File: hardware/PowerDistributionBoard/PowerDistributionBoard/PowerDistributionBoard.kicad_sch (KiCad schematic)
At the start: 117 parts, among them J1 Battery, J10 MOTOR2_PWR, J11 Router, J2 FAN 1, J3 FAN 2, J4 FAN 3, J5 FAN 4, J6 Inverter, J7 Control Board, J8 Conn_01x02, J9 MOTOR1_PWR, Q1 Q_NMOS_GDS, Q10 TK100E10N1,S1X, Q2 Q_NPN_EBC, Q3 Q_NMOS_GSD, Q4 Q_NMOS_GSD, Q5 Q_NPN_EBC, Q6 Q_NMOS_GSD, Q7 Q_NMOS_GSD, Q8 DMN62D0U-13, Q9 TK100E10N1,S1X, SW1 SW_SPDT, U1 LT1641-1, U2 MAX6643LBBAEET, U3 MAX6643LBBAEET, U4 MC74HC20ADG, U5 KSTW004A2B41Z, U6 AP2210N-3.3TRG1, U7 R-78B9.0-1.0

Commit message: Power Board Schematic Revision Done, Fix Lora Symbol and Update Control Board Routing
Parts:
- removed F1: 1A, PDBLib:0679L1000-05, symbol Device:Fuse
- added F?: 2A, PDBLib:3557-2, symbol Device:Fuse
- added F? (x2): 10A, PDBLib:3557-2, symbol Device:Fuse
- added F?: 25A, PDBLib:3557-2, symbol Device:Fuse
- added F? (x2): 1A, PDBLib:3557-2, symbol Device:Fuse
- C3: value 100p -> 1n
- D10, D9: footprint Package_TO_SOT_THT:TO-247-2_Horizontal_TabDown -> PDBLib:VS-15AWL06FNTR-M3; Digikey APT60DQ60BG-ND -> VS-15AWL06FNTR-M3GICT-ND; LCSC (none) -> C2838505
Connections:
- net +12V: now also F?.2; no longer D?.1 (K), J7.1 (Pin_1)
- net +48V: now also F?.2, F?.2, F?.2, F?.2; no longer C17.1, D10.1 (K), D9.1 (K), D?.1 (K), J10.1 (Pin_1), J6.1 (Pin_1), J9.1 (Pin_1)
- net +9V: now also F?.2; no longer D?.1 (K), J11.1 (Pin_1)
- net at C9.1, U5.1 (VIN+): now also F?.1
- new net: D?.1 (K), F?.1, J7.1 (Pin_1)
- new net: D10.1 (K), F?.1, J10.1 (Pin_1)
- new net: C17.1, D?.1 (K), F?.1, J6.1 (Pin_1)
- new net: D9.1 (K), F?.1, J9.1 (Pin_1)
- new net: D?.1 (K), F?.1, J11.1 (Pin_1)
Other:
- note added: "REVIEW V0.2"
- note removed: "REVIEW V0.1"
- moved on the sheet: C17, D?, J11, J6, J7

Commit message: PDB Layout
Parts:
- added R44: 4.7k, Resistor_SMD:R_0805_2012Metric, symbol Device:R_US
- C17, C9: footprint Capacitor_THT:CP_Radial_D12.5mm_P5.00mm -> Capacitor_THT:CP_Radial_D10.0mm_P5.00mm; Digikey 4191-PF2D330MCE1212F3-ND -> 1189-2207-ND; LCSC (none) -> C159830
- J11, J7: footprint Connector_Molex:Molex_Micro-Fit_3.0_43650-0200_1x02_P3.00mm_Horizontal -> Connector_Molex:Molex_Micro-Fit_3.0_43650-0215_1x02_P3.00mm_Vertical; Digikey WM1860-ND -> WM1917-ND
- R33: value 1k -> 4.7k
- gave numbers to parts that had none: 11
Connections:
- net ESTOP: now also R44.2
- net GND: now also R44.1

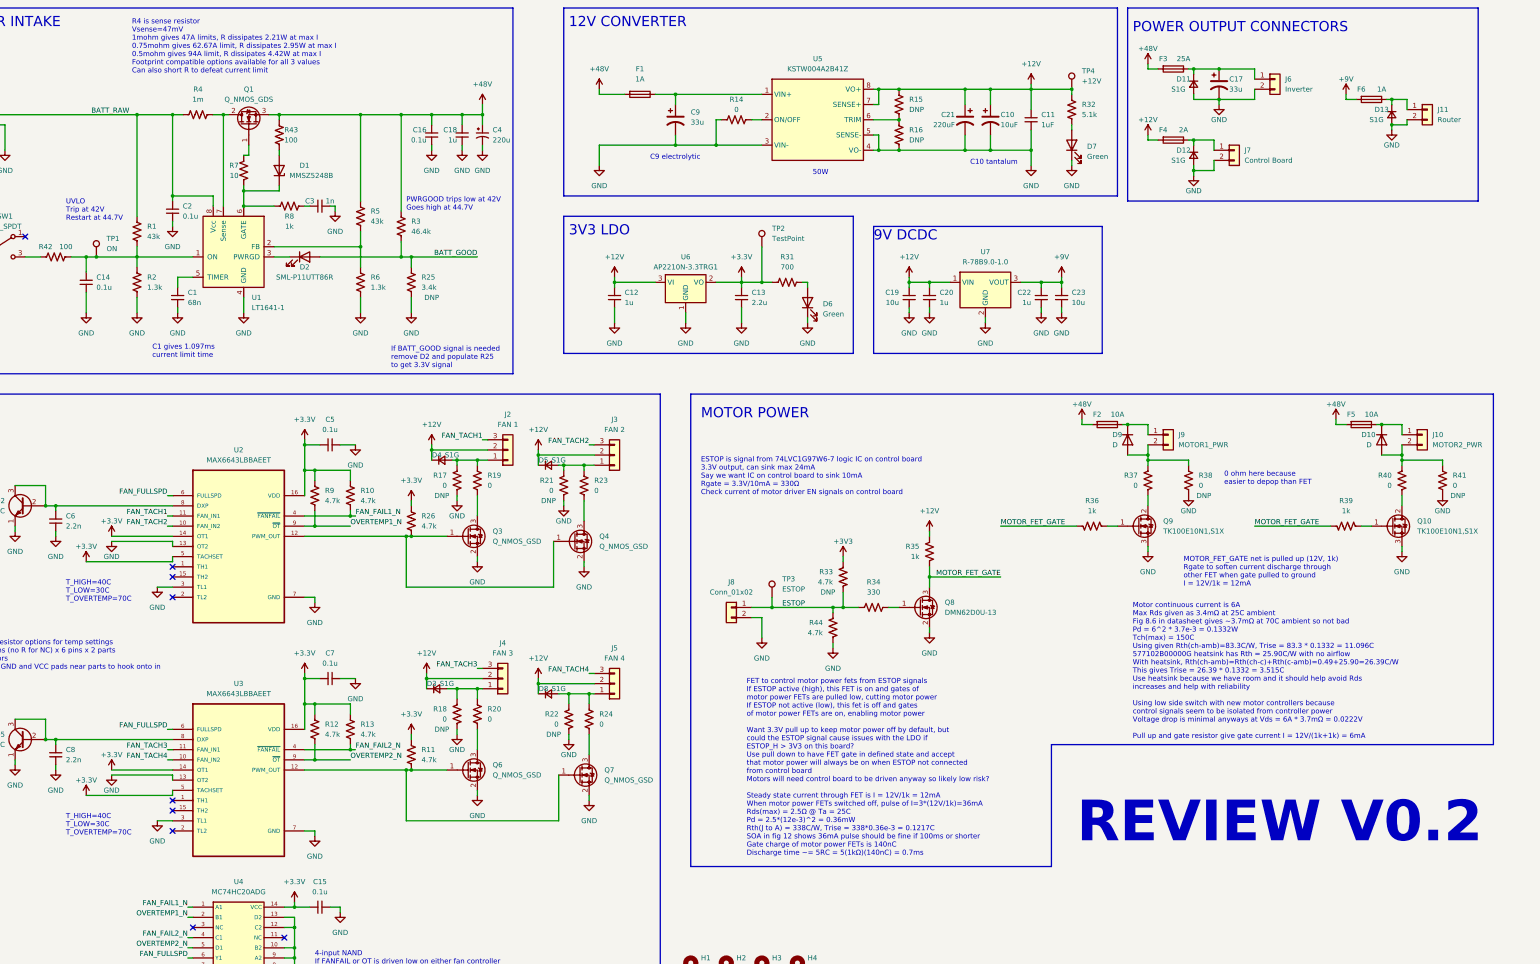
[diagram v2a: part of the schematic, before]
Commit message: PDB routing V2 first pass
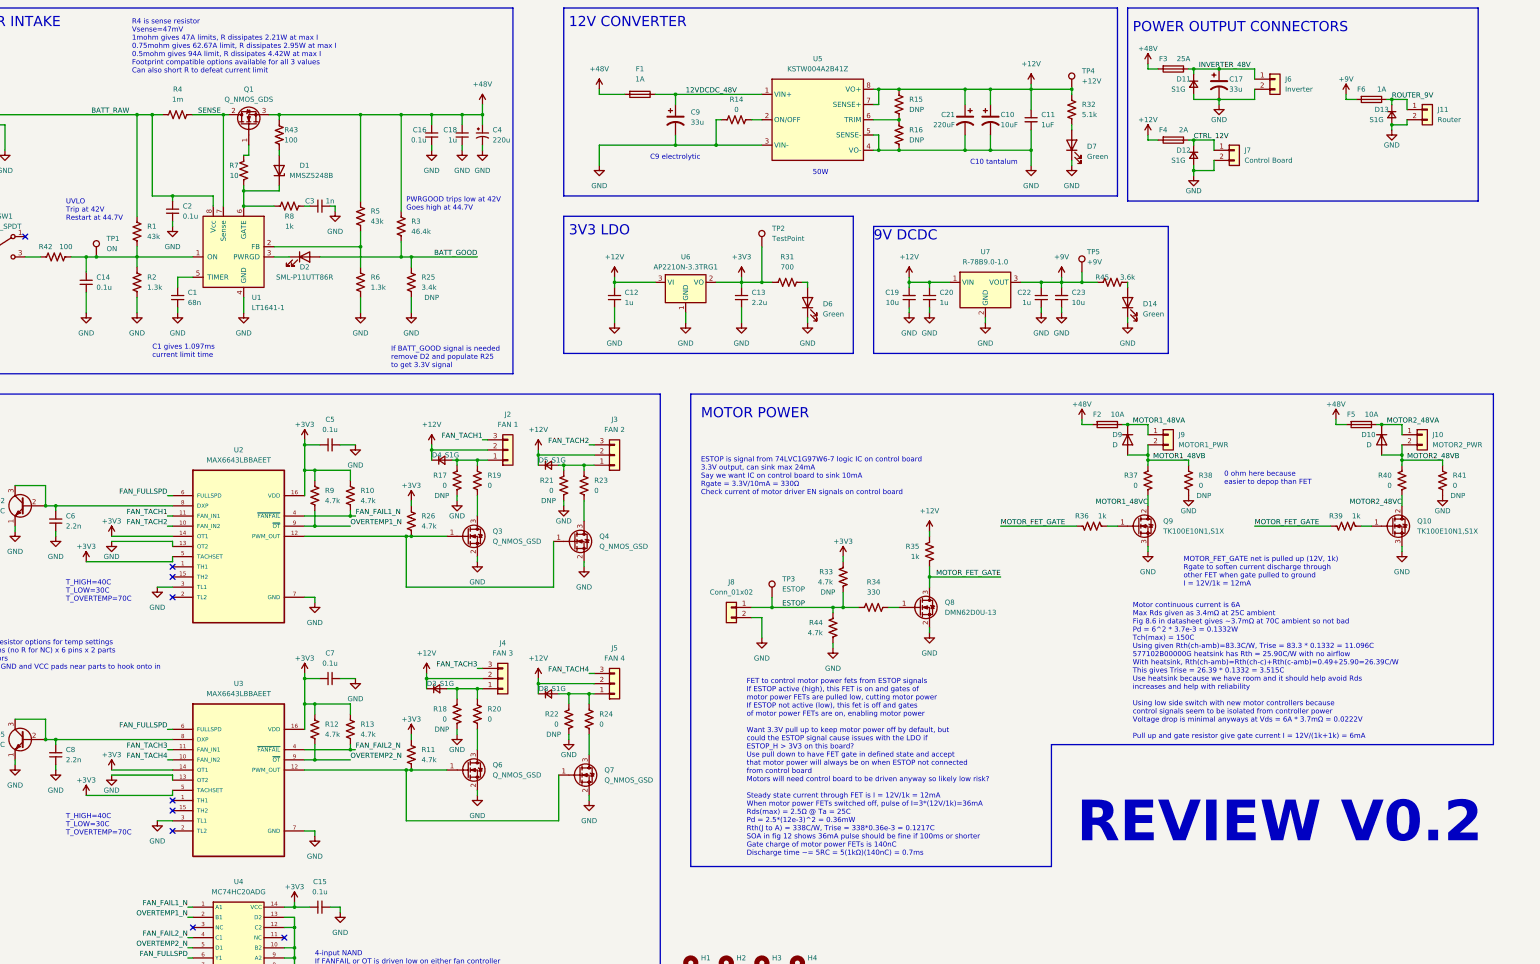
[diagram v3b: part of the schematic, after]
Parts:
- added D14: Green, LED_SMD:LED_0805_2012Metric_Pad1.15x1.40mm_HandSolder, symbol Device:LED
- added R45: 3.6k, Resistor_SMD:R_0805_2012Metric, symbol Device:R_US
- added TP5: +9V, TestPoint:TestPoint_Pad_D1.0mm, symbol Connector:TestPoint
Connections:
- net +3.3V is gone; now on net +3V3: C13.1, C15.1, C5.2, C7.2, R10.1, R11.1, R12.1, R13.1, R26.1, R31.2, R9.1, TP2.1, U2.14 (OT1), U2.16 (VDD), U2.5 (TACHSET), U3.14 (OT1), U3.16 (VDD), U3.5 (TACHSET), U4.14 (VCC), U6.2 (VO)
- net +9V: now also R45.2, TP5.1
- net GND: now also D14.1 (K)
- net CTRL_12V: now reaches D12.1 (K), F4.1, J7.1 (Pin_1)
- net MOTOR2_48VA: now reaches D10.1 (K), F5.1, J10.1 (Pin_1)
- net INVERTER_48V: now reaches C17.1, D11.1 (K), F3.1, J6.1 (Pin_1)
- net MOTOR2_48VC: now reaches Q10.2 (D), R40.1
- net MOTOR2_48VB: now reaches D10.2 (A), J10.2 (Pin_2), R40.2, R41.1
- net ROUTER_9V: now reaches D13.1 (K), F6.1, J11.1 (Pin_1)
- net SENSE: now reaches Q1.2 (D), R4.1, U1.7 (Sense)
- net MOTOR1_48VA: now reaches D9.1 (K), F2.1, J9.1 (Pin_1)
- net 12VDCDC_48V: now reaches C9.1, F1.1, U5.1 (VIN+)
- net MOTOR1_48VC: now reaches Q9.2 (D), R37.1
- net MOTOR1_48VB: now reaches D9.2 (A), J9.2 (Pin_2), R37.2, R38.1
- new net: D14.2 (A), R45.1
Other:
- moved on the sheet: R4

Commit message: Last things
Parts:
- U1: footprint Package_SO:SOIC-8_3.9x4.9mm_P1.27mm -> PDBLib:LT1641-1CS8#TRPBF
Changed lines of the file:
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@@
       (effects (font (size 1.27 1.27)) (justify left))
     )
-    (property "Footprint" "Package_SO:SOIC-8_3.9x4.9mm_P1.27mm" (id 2) (at 90.17 91.44 0)
+    (property "Footprint" "PDBLib:LT1641-1CS8#TRPBF" (id 2) (at 90.17 91.44 0)
       (effects (font (size 1.27 1.27)) hide)
     )
@@
     )
     (path "/a957320b-6e63-458d-80eb-4ce3c9404919"
-      (reference "U1") (unit 1) (value "LT1641-1") (footprint "Package_SO:SOIC-8_3.9x4.9mm_P1.27mm")
+      (reference "U1") (unit 1) (value "LT1641-1") (footprint "PDBLib:LT1641-1CS8#TRPBF")
     )
     (path "/efe103fd-3ce0-4747-adbc-34ad97d64139"

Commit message: PDB Assembly PNs
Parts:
- C1: LCSC (none) -> C113842; Voltage (none) -> 44V
- C11, C12: LCSC (none) -> C116352; Voltage (none) -> 12V
- C13: LCSC (none) -> C107366; Voltage (none) -> 3.3V
- C14, C2: LCSC (none) -> C28233; Voltage (none) -> 48V
- C15, C5, C7: LCSC (none) -> C597440; Voltage (none) -> 3.3V
- C16, C18: LCSC (none) -> C28233
- C19, C23: LCSC (none) -> C237493
- C20, C22: LCSC (none) -> C116352
- C21: LCSC (none) -> C88729
- C3: LCSC (none) -> C16005; Voltage (none) -> 68V
- C6, C8: LCSC (none) -> C1728; Voltage (none) -> 0.8V
- J2, J3, J4, J5: LCSC (none) -> C471416
- Q2, Q5: LCSC (none) -> C79629
- R1, R5: LCSC (none) -> C137524
- R10, R11, R12, R13, R26, R44, R9: LCSC (none) -> C140869
- R14, R19, R20, R23, R24: LCSC (none) -> C237773
- R15, R16: value DNP -> ?; DNP (none) -> DNP
- R2, R6: LCSC (none) -> C137582
- R27, R28, R29, R30: DNP (none) -> DNP
- R3: LCSC (none) -> C317450
- R31: LCSC (none) -> C483228
- R32: LCSC (none) -> C84375
- R34: LCSC (none) -> C105878
- R35, R36, R39, R8: LCSC (none) -> C510097
- R42, R43: LCSC (none) -> C105577
- R45: LCSC (none) -> C137533
- R7: LCSC (none) -> C2074472
- SW1: LCSC (none) -> C273394

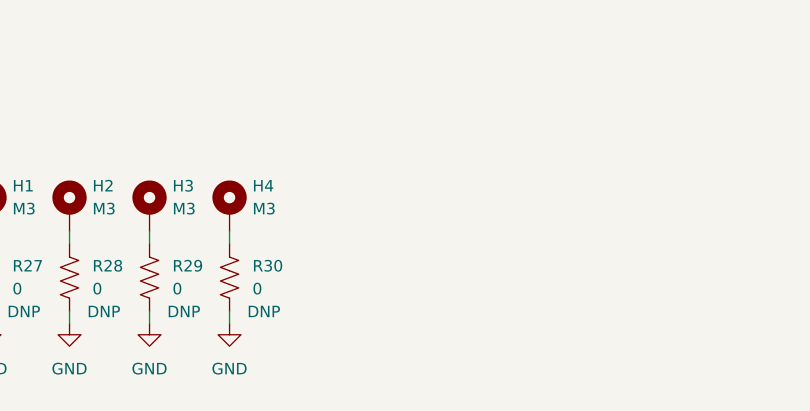
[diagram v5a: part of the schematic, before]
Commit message: Finish adding assembly PNs
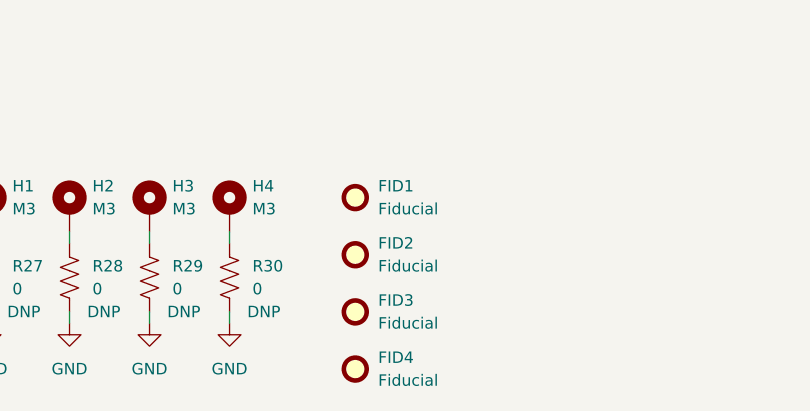
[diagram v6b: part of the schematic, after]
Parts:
- added FID1, FID2, FID3, FID4: Fiducial, Fiducial:Fiducial_1mm_Mask2mm, symbol Mechanical:Fiducial

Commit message: Build Files
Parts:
- C10: value 10uF -> 10u
- C11: value 1uF -> 1u
- C21: value 220uF -> 220u
- R15, R16: value ? -> DNP
- R17, R18, R21, R22, R27, R28, R29, R30, R38, R41: value 0 -> 0_DNP
- R25: value 3.4k -> 3.4k_DNP
- R33: value 4.7k -> 4.7k_DNP
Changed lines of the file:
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@@
       (effects (font (size 1.27 1.27)) (justify left))
     )
-    (property "Value" "0" (id 1) (at 393.7 135.8899 0)
+    (property "Value" "0_DNP" (id 1) (at 393.7 135.8899 0)
       (effects (font (size 1.27 1.27)) (justify left))
     )
@@
       (effects (font (size 1.27 1.27)) (justify right))
     )
-    (property "Value" "0" (id 1) (at 168.91 137.1599 0)
+    (property "Value" "0_DNP" (id 1) (at 168.91 137.1599 0)
       (effects (font (size 1.27 1.27)) (justify right))
     )
@@
       (effects (font (size 1.27 1.27)) (justify left))
     )
-    (property "Value" "220uF" (id 1) (at 269.24 45.72 0)
+    (property "Value" "220u" (id 1) (at 269.24 45.72 0)
       (effects (font (size 1.27 1.27)) (justify left))
     )
@@
       (effects (font (size 1.27 1.27)) (justify right))
     )
-    (property "Value" "0" (id 1) (at 142.24 135.8899 0)
+    (property "Value" "0_DNP" (id 1) (at 142.24 135.8899 0)
       (effects (font (size 1.27 1.27)) (justify right))
     )
@@
       (effects (font (size 1.27 1.27)) (justify left))
     )
-    (property "Value" "0" (id 1) (at 205.74 265.4299 0)
+    (property "Value" "0_DNP" (id 1) (at 205.74 265.4299 0)
       (effects (font (size 1.27 1.27)) (justify left))
     )
@@
       (effects (font (size 1.27 1.27)) (justify left))
     )
-    (property "Value" "?" (id 1) (at 257.81 41.9099 0)
+    (property "Value" "DNP" (id 1) (at 257.81 41.9099 0)
       (effects (font (size 1.27 1.27)) (justify left))
     )
@@
       (effects (font (size 1.27 1.27)) (justify left))
     )
-    (property "Value" "0" (id 1) (at 214.63 265.4299 0)
+    (property "Value" "0_DNP" (id 1) (at 214.63 265.4299 0)
       (effects (font (size 1.27 1.27)) (justify left))
     )
@@
       (effects (font (size 1.27 1.27)) (justify left))
     )
-    (property "Value" "1uF" (id 1) (at 290.83 45.7262 0)
+    (property "Value" "1u" (id 1) (at 290.83 45.7262 0)
       (effects (font (size 1.27 1.27)) (justify left))
     )
@@
       (effects (font (size 1.27 1.27)) (justify right))
     )
-    (property "Value" "0" (id 1) (at 142.24 194.3099 0)
+    (property "Value" "0_DNP" (id 1) (at 142.24 194.3099 0)
       (effects (font (size 1.27 1.27)) (justify right))
     )
@@
       (effects (font (size 1.27 1.27)) (justify right))
     )
-    (property "Value" "4.7k" (id 1) (at 238.76 160.0199 0)
+    (property "Value" "4.7k_DNP" (id 1) (at 238.76 160.0199 0)
       (effects (font (size 1.27 1.27)) (justify right))
     )
@@
       (effects (font (size 1.27 1.27)) (justify left))
     )
-    (property "Value" "0" (id 1) (at 232.41 265.4299 0)
+    (property "Value" "0_DNP" (id 1) (at 232.41 265.4299 0)
       (effects (font (size 1.27 1.27)) (justify left))
     )
@@
       (effects (font (size 1.27 1.27)) (justify left))
     )
-    (property "Value" "3.4k" (id 1) (at 135.89 86.3599 0)
+    (property "Value" "3.4k_DNP" (id 1) (at 135.89 86.3599 0)
       (effects (font (size 1.27 1.27)) (justify left))
     )
@@
       (effects (font (size 1.27 1.27)) (justify left))
     )
-    (property "Value" "0" (id 1) (at 223.52 265.4299 0)
+    (property "Value" "0_DNP" (id 1) (at 223.52 265.4299 0)
       (effects (font (size 1.27 1.27)) (justify left))
     )
@@
       (effects (font (size 1.27 1.27)) (justify left))
     )
-    (property "Value" "10uF" (id 1) (at 280.67 45.72 0)
+    (property "Value" "10u" (id 1) (at 280.67 45.72 0)
       (effects (font (size 1.27 1.27)) (justify left))
     )
@@
       (effects (font (size 1.27 1.27)) (justify right))
     )
-    (property "Value" "0" (id 1) (at 170.18 195.5799 0)
+    (property "Value" "0_DNP" (id 1) (at 170.18 195.5799 0)
       (effects (font (size 1.27 1.27)) (justify right))
     )
@@
       (effects (font (size 1.27 1.27)) (justify left))
     )
-    (property "Value" "0" (id 1) (at 330.2 135.8899 0)
+    (property "Value" "0_DNP" (id 1) (at 330.2 135.8899 0)
       (effects (font (size 1.27 1.27)) (justify left))
     )
@@
       (effects (font (size 1.27 1.27)) (justify left))
     )
-    (property "Value" "?" (id 1) (at 257.81 49.5299 0)
+    (property "Value" "DNP" (id 1) (at 257.81 49.5299 0)
       (effects (font (size 1.27 1.27)) (justify left))
     )
@@
     )
     (path "/c6600d8c-a2e6-4bda-84d0-ffc085ab6026"
-      (reference "C10") (unit 1) (value "10uF") (footprint "Capacitor_SMD:C_1206_3216Metric")
+      (reference "C10") (unit 1) (value "10u") (footprint "Capacitor_SMD:C_1206_3216Metric")
     )
     (path "/60aa87ee-eb1c-415c-b9d1-3eed3e8e16ed"
-      (reference "C11") (unit 1) (value "1uF") (footprint "Capacitor_SMD:C_0805_2012Metric")
+      (reference "C11") (unit 1) (value "1u") (footprint "Capacitor_SMD:C_0805_2012Metric")
     )
     (path "/cf263375-0958-450b-9319-84ce34c5deb9"
@@
     )
     (path "/356ceeaf-91ee-4761-b7b3-f4be80f2f7fe"
-      (reference "C21") (unit 1) (value "220uF") (footprint "Capacitor_THT:CP_Radial_D6.3mm_P2.50mm")
+      (reference "C21") (unit 1) (value "220u") (footprint "Capacitor_THT:CP_Radial_D6.3mm_P2.50mm")
     )
     (path "/636f1c9e-3a0e-463a-9dc5-831043a96db2"
@@
     )
     (path "/4e656a93-5e7d-4f63-a0a6-bd0926b77c69"
-      (reference "R15") (unit 1) (value "?") (footprint "Resistor_SMD:R_0805_2012Metric")
+      (reference "R15") (unit 1) (value "DNP") (footprint "Resistor_SMD:R_0805_2012Metric")
     )
     (path "/edfe4000-4194-467b-9afa-88182bfd1054"
-      (reference "R16") (unit 1) (value "?") (footprint "Resistor_SMD:R_0805_2012Metric")
+      (reference "R16") (unit 1) (value "DNP") (footprint "Resistor_SMD:R_0805_2012Metric")
     )
     (path "/4091bd75-2a51-4bf8-aefb-22f381d0c828"
-      (reference "R17") (unit 1) (value "0") (footprint "Resistor_SMD:R_0805_2012Metric")
+      (reference "R17") (unit 1) (value "0_DNP") (footprint "Resistor_SMD:R_0805_2012Metric")
     )
     (path "/64b5813c-a815-406f-be64-5985addfa0de"
-      (reference "R18") (unit 1) (value "0") (footprint "Resistor_SMD:R_0805_2012Metric")
+      (reference "R18") (unit 1) (value "0_DNP") (footprint "Resistor_SMD:R_0805_2012Metric")
     )
     (path "/a93870d3-690e-4161-8c65-f4e299ddb90a"
@@
     )
     (path "/32026dd4-72a5-4577-b5b3-d591b0cf3716"
-      (reference "R21") (unit 1) (value "0") (footprint "Resistor_SMD:R_0805_2012Metric")
+      (reference "R21") (unit 1) (value "0_DNP") (footprint "Resistor_SMD:R_0805_2012Metric")
     )
     (path "/c8046250-debd-49d0-aceb-427635568de6"
-      (reference "R22") (unit 1) (value "0") (footprint "Resistor_SMD:R_0805_2012Metric")
+      (reference "R22") (unit 1) (value "0_DNP") (footprint "Resistor_SMD:R_0805_2012Metric")
     )
     (path "/6c0fa229-3407-4345-9754-f493aa4dad83"
@@
     )
     (path "/9573399e-7ff0-4f69-b464-4daa0d8221d3"
-      (reference "R25") (unit 1) (value "3.4k") (footprint "Resistor_SMD:R_0805_2012Metric")
+      (reference "R25") (unit 1) (value "3.4k_DNP") (footprint "Resistor_SMD:R_0805_2012Metric")
     )
     (path "/a93569f7-e4ea-41a9-b324-7d24aee952fe"
@@
     )
     (path "/45564d51-6638-463a-b07c-3fcb15698204"
-      (reference "R27") (unit 1) (value "0") (footprint "Resistor_SMD:R_0805_2012Metric")
+      (reference "R27") (unit 1) (value "0_DNP") (footprint "Resistor_SMD:R_0805_2012Metric")
     )
     (path "/59e586fb-6067-494c-a7cd-13415c7c1662"
-      (reference "R28") (unit 1) (value "0") (footprint "Resistor_SMD:R_0805_2012Metric")
+      (reference "R28") (unit 1) (value "0_DNP") (footprint "Resistor_SMD:R_0805_2012Metric")
     )
     (path "/a5a1a52b-bae0-48a1-b635-e006557271b7"
-      (reference "R29") (unit 1) (value "0") (footprint "Resistor_SMD:R_0805_2012Metric")
+      (reference "R29") (unit 1) (value "0_DNP") (footprint "Resistor_SMD:R_0805_2012Metric")
     )
     (path "/8385da97-26e3-4ef5-b699-1e6f95a10370"
-      (reference "R30") (unit 1) (value "0") (footprint "Resistor_SMD:R_0805_2012Metric")
+      (reference "R30") (unit 1) (value "0_DNP") (footprint "Resistor_SMD:R_0805_2012Metric")
     )
     (path "/5b3e6555-2729-4558-b6d6-c440e2a99da8"
@@
     )
     (path "/7ec3f725-ff89-4ee8-9e58-e2cfb79be754"
-      (reference "R33") (unit 1) (value "4.7k") (footprint "Resistor_SMD:R_0805_2012Metric")
+      (reference "R33") (unit 1) (value "4.7k_DNP") (footprint "Resistor_SMD:R_0805_2012Metric")
     )
     (path "/024ae17b-030e-469b-89db-adb2b355ce4f"
@@
     )
     (path "/e6543b95-5e66-4ad4-ac00-271fc3300f68"
-      (reference "R38") (unit 1) (value "0") (footprint "Resistor_SMD:R_2512_6332Metric")
+      (reference "R38") (unit 1) (value "0_DNP") (footprint "Resistor_SMD:R_2512_6332Metric")
     )
     (path "/4202116a-c026-4093-8af6-baf59b34b538"
@@
     )
     (path "/301a9f9c-37c4-4794-baf4-8c41e63178f2"
-      (reference "R41") (unit 1) (value "0") (footprint "Resistor_SMD:R_2512_6332Metric")
+      (reference "R41") (unit 1) (value "0_DNP") (footprint "Resistor_SMD:R_2512_6332Metric")
     )
     (path "/0c405a71-c76c-4c01-a2c2-4fcec38a4a35"
